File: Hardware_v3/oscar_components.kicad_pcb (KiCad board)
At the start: 4 copper layers, 71 x 100 mm, 65 parts, among them J1 SWD_Header, J10 USB_C_Receptacle, J11 MIDI_OUT, J2 ChannelA_In, J3 ChannelB_In, J4 ChannelC_In, J5 ChA_Buff_Out, J6 ChB_Buff_Out, J7 ChC_Buff_Out, J8 MIDI_IN, J9 Eurorack_10_pin_power, SW1 Left_Encoder, SW2 Right_Encoder, SW3 Reset_Button, SW4 Menu_Button, U1 STM32F446RETx, U2 ILI9341_SPI_Daughterboard, U3 MCP6004, U4 TL074, U5 LT1117-3.3, U6 6N137, Y1 8MHz

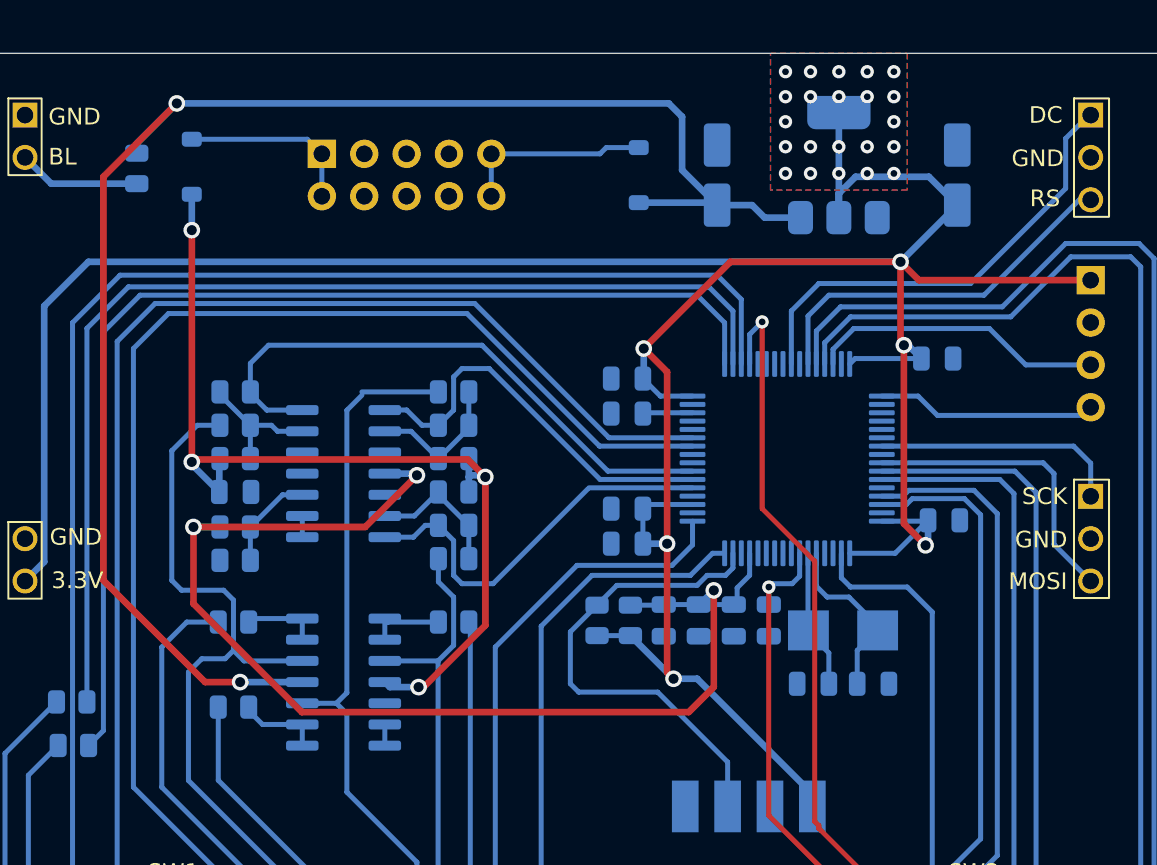
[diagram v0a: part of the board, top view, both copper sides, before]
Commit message: Folder reorganisation
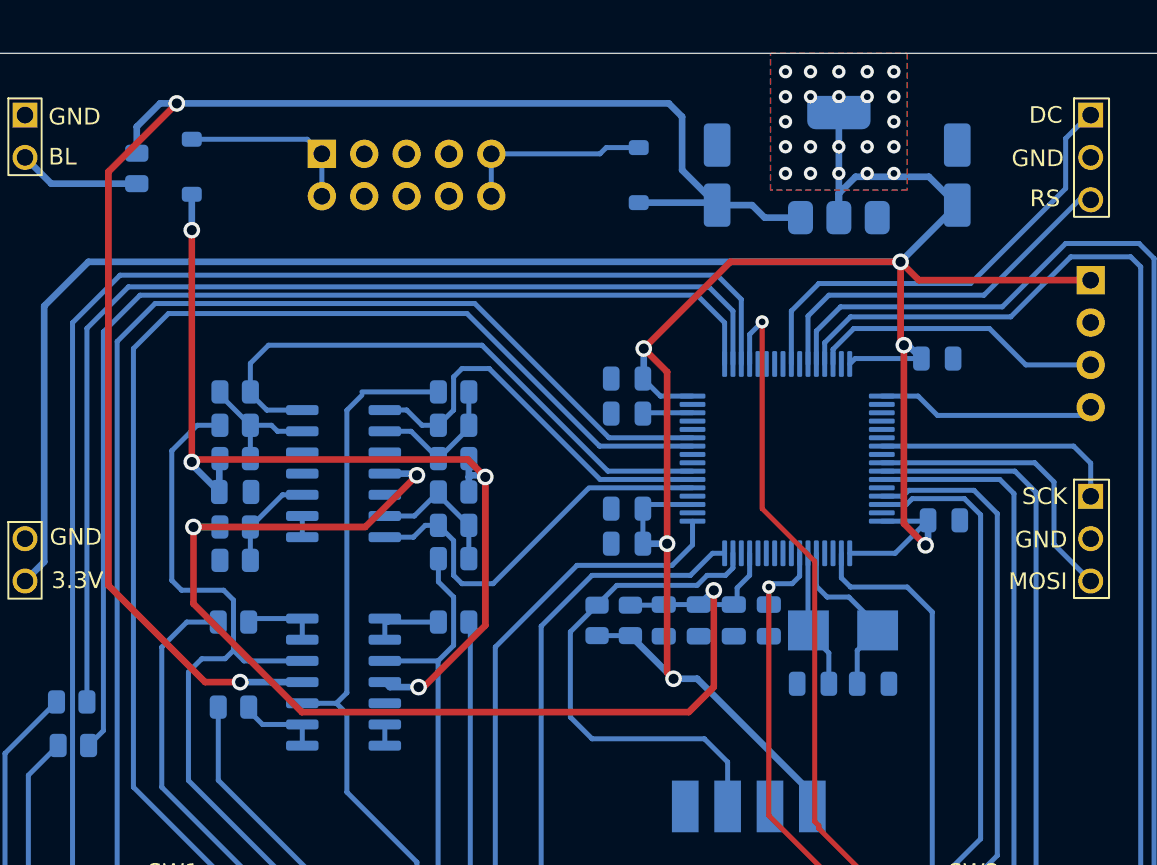
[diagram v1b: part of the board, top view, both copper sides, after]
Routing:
- net /MIDI_RX: track 29.4 -> 30.5 mm
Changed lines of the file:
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@@
 	)
 	(segment
-		(start 113.1 87.7)
-		(end 107 81.6)
+		(start 107.3 81.9)
+		(end 107.3 57.1)
 		(width 0.4)
 		(layer "F.Cu")
@@
 	)
 	(segment
-		(start 107 81.6)
-		(end 107 57.4)
+		(start 113.1 87.7)
+		(end 107.3 81.9)
 		(width 0.4)
 		(layer "F.Cu")
@@
 	)
 	(segment
-		(start 107 57.4)
+		(start 107.3 57.1)
 		(end 111.4 53)
 		(width 0.4)
@@
 	)
 	(segment
-		(start 109 55.4)
-		(end 111.4 53)
-		(width 0.4)
-		(layer "B.Cu")
-		(net 7)
-	)
-	(segment
 		(start 143.8 59.1)
 		(end 145.9 59.1)
@@
 	)
 	(segment
+		(start 109 54.4)
+		(end 110.4 53)
+		(width 0.4)
+		(layer "B.Cu")
+		(net 7)
+	)
+	(segment
 		(start 111.4 53)
 		(end 140.9 53)
@@
 	)
 	(segment
+		(start 110.4 53)
+		(end 111.4 53)
+		(width 0.4)
+		(layer "B.Cu")
+		(net 7)
+	)
+	(segment
 		(start 109 55.9875)
-		(end 109 55.4)
+		(end 109 54.4)
 		(width 0.4)
 		(layer "B.Cu")
@@
 	)
 	(segment
-		(start 143.2 81.3)
-		(end 144.30312 81.3)
+		(start 136.3 91.1)
+		(end 135 89.8)
 		(width 0.3)
 		(layer "B.Cu")
@@
 	)
 	(segment
-		(start 142.6 81.9)
-		(end 143.2 81.3)
+		(start 143.2 81.3)
+		(end 144.30312 81.3)
 		(width 0.3)
 		(layer "B.Cu")
@@
 	)
 	(segment
-		(start 140.235 88.3)
-		(end 135.5 88.3)
+		(start 142.6 81.9)
+		(end 143.2 81.3)
 		(width 0.3)
 		(layer "B.Cu")
@@
 	)
 	(segment
-		(start 144.43 95.155)
-		(end 144.43 92.495)
+		(start 144.30312 81.3)
+		(end 144.75 80.85312)
 		(width 0.3)
 		(layer "B.Cu")
@@
 	)
 	(segment
-		(start 144.30312 81.3)
-		(end 144.75 80.85312)
+		(start 135 89.8)
+		(end 135 84.6875)
 		(width 0.3)
 		(layer "B.Cu")
@@
 	)
 	(segment
-		(start 135 87.8)
-		(end 135 84.6875)
+		(start 144.43 92.495)
+		(end 143.035 91.1)
 		(width 0.3)
 		(layer "B.Cu")
@@
 	)
 	(segment
-		(start 144.43 92.495)
-		(end 140.235 88.3)
+		(start 136.6 83.0875)
+		(end 137.7875 81.9)
 		(width 0.3)
 		(layer "B.Cu")
@@
 	)
 	(segment
-		(start 135.5 88.3)
-		(end 135 87.8)
+		(start 135 84.6875)
+		(end 136.6 83.0875)
 		(width 0.3)
 		(layer "B.Cu")
@@
 	)
 	(segment
-		(start 136.6 83.0875)
-		(end 137.7875 81.9)
+		(start 143.035 91.1)
+		(end 136.3 91.1)
 		(width 0.3)
 		(layer "B.Cu")
@@
 	)
 	(segment
-		(start 135 84.6875)
-		(end 136.6 83.0875)
+		(start 144.75 80.85312)
+		(end 144.75 79.975)
 		(width 0.3)
 		(layer "B.Cu")
@@
 	)
 	(segment
-		(start 144.75 80.85312)
-		(end 144.75 79.975)
+		(start 144.43 95.155)
+		(end 144.43 92.495)
 		(width 0.3)
 		(layer "B.Cu")
@@
 	)
 	(segment
-		(start 164 79.44)
-		(end 164 75.2)
+		(start 166.2 81.64)
+		(end 164 79.44)
 		(width 0.3)
 		(layer "B.Cu")
@@
 	)
 	(segment
-		(start 163.35 74.55)
-		(end 153.675 74.55)
+		(start 164 75.7)
+		(end 162.85 74.55)
 		(width 0.3)
 		(layer "B.Cu")
@@
 	)
 	(segment
-		(start 164 75.2)
-		(end 163.35 74.55)
+		(start 164 79.44)
+		(end 164 75.7)
 		(width 0.3)
 		(layer "B.Cu")
@@
 	)
 	(segment
-		(start 166.2 81.64)
-		(end 164 79.44)
+		(start 162.85 74.55)
+		(end 153.675 74.55)
 		(width 0.3)
 		(layer "B.Cu")

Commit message: PCB Layout
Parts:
- added TP1: TestPoint, Custom_Footprints:1.3mm_Test_Point, F.Cu at (105.9, 60.4)
- added TP2: TestPoint, Custom_Footprints:1.3mm_Test_Point, F.Cu at (110.1, 60.4)
- added TP3: TestPoint, Custom_Footprints:1.3mm_Test_Point, F.Cu at (162.3, 140.0)
- added TP4: TestPoint, Custom_Footprints:1.3mm_Test_Point, F.Cu at (105.9, 51.9)
- added TP5: TestPoint, Custom_Footprints:1.3mm_Test_Point, F.Cu at (102.0, 60.4)
- J10: renamed from J11; value MIDI_OUT -> MIDI_THROUGH
- moved C15 3.50 mm to (115.0, 79.8)
- moved R10 3.50 mm to (128.1, 75.8)
- moved R11 3.50 mm to (115.0, 81.9)
- moved R12 3.50 mm to (115.0, 83.9)
- moved R13 3.50 mm to (128.1, 87.6)
- moved R14 3.50 mm to (114.9, 87.6)
- moved R15 3.50 mm to (114.9, 92.7)
- moved R2 3.50 mm to (128.1, 79.8)
- moved R3 3.50 mm to (128.1, 83.8)
- moved R4 3.50 mm to (115.0, 77.8)
- moved R5 3.50 mm to (115.0, 75.8)
- moved R6 3.50 mm to (128.1, 77.8)
- moved R7 3.50 mm to (128.1, 73.8)
- moved R8 3.50 mm to (128.1, 81.8)
- moved R9 3.50 mm to (115.0, 73.8)
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- renumbered C8 to C1, C6 to C10, C16 to C11, C7 to C12, C10 to C14, C11 to C15, C12 to C2, C1 to C3, C2 to C4, C3 to C5, C4 to C6, C9 to C7, C14 to C8, C5 to C9, D4 to D3, D3 to D4, J10 to J11, J9 to J2, J4 to J3, J2 to J4, J3 to J5, J7 to J6, J5 to J7, J6 to J8, J8 to J9, R13 to R1, R9 to R10, R16 to R11, R17 to R12, R10 to R13, R11 to R14, R12 to R15, R14 to R16, R15 to R17, R1 to R2, R2 to R3, R3 to R4, R4 to R5, R5 to R6, R6 to R7, R7 to R8, R8 to R9, SW3 to SW1, SW4 to SW2, SW1 to SW3, SW2 to SW4, U5 to U1, U1 to U3, U3 to U5
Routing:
- net +3.3V: track 202.1 -> 212.3 mm
- net -12V: track 58.4 -> 65.1 mm
- net +12V: track 96.1 -> 101.2 mm
- net /CHC_In: track 65.7 -> 61.6 mm
- net /CHB_Out: track 64.1 -> 60.0 mm
- net /CHA_In: track 86.0 -> 82.1 mm
- net /CHB_In: track 72.5 -> 68.6 mm
- net /CHA_Out: track 79.2 -> 75.4 mm
- net /CHC_Out: track 72.9 -> 69.4 mm
- net /ChC_Button: track 58.8 -> 56.4 mm
- net /ChA_Button: track 107.2 -> 104.8 mm
- net /L_ENC_BTN: track 73.1 -> 70.8 mm
- net /ChB_LED: track 66.5 -> 64.6 mm
- net +3.3VA: track 74.2 -> 76.0 mm
- net /LCD_SCK: track 14.9 -> 13.1 mm
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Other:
- board text added: "-12V"
- board text added: "12V"
- board text added: "3V3"
- board text added: "GND"
- board text added: "Oscar v3 Mountjoy Modular 2025"
- board text removed: "Oscar v3 Mountjoy Modular"

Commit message: Started working on panel
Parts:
- added J12: Debug, Connector_PinHeader_2.54mm:PinHeader_1x03_P2.54mm_Vertical, B.Cu at (166.0, 92.8)
- SW1: footprint Button_Switch_THT:SW_PUSH_6mm -> Custom_Footprints:SW_PUSH_6mm_aligned
- moved TP4 17.7 mm to (102.0, 69.2)
- moved SW1 3.70 mm to (150.4, 131.2)
- moved SW3 3.20 mm to (111.2, 105.0)
- moved SW4 3.20 mm to (159.2, 105.0)
- moved BTN1 2.60 mm to (109.4, 120.0)
- moved BTN2 2.60 mm to (124.5, 120.0)
- moved BTN3 2.60 mm to (139.4, 120.0)
- moved J3 0.80 mm to (139.4, 132.0)
- moved J4 0.80 mm to (109.4, 132.0)
- moved J5 0.80 mm to (124.4, 132.0)
- moved D4 0.30 mm to (156.4, 137.9)
- moved J11 0.30 mm to (150.5, 144.1)
- moved U2 0.20 mm to (102.1, 53.7)
- moved R19 0.10 mm to (105.1, 91.5)
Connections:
- U3 pad 51: unconnected-(U3-PC10-Pad51) -> /DEBUG1
- U3 pad 52: unconnected-(U3-PC11-Pad52) -> /DEBUG2
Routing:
- net /DEBUG1: track 0.00 -> 34.3 mm
- net /DEBUG2: track 0.00 -> 30.0 mm
- net /ChB_Button: track 107.8 -> 100.1 mm
- net /L_ENC_DN: track 85.0 -> 77.4 mm
- net Net-(BTN2-A): track 48.2 -> 53.9 mm
- net /L_ENC_UP: track 92.9 -> 88.9 mm
- net /L_ENC_BTN: track 70.8 -> 67.3 mm
- net /R_ENC_BTN: track 23.9 -> 20.7 mm
- net /R_ENC_UP: track 50.5 -> 47.3 mm
- net /R_ENC_DN: track 58.1 -> 55.1 mm
- net /ChA_Button: track 104.8 -> 102.0 mm
- net Net-(BTN3-A): track 7.11 -> 4.51 mm
- net +3.3V: track 212.3 -> 214.6 mm
- net /CHA_Out: track 75.4 -> 77.5 mm
- net /ChC_Button: track 56.4 -> 54.5 mm
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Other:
- board text added: "Debug"
- board text added: "PC10"
- board text added: "PC11"

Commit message: Control Layout change
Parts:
- SW2: footprint Button_Switch_THT:SW_PUSH_6mm -> Custom_Footprints:Low-Profile_Push_Button
- moved J9 54.2 mm to (107.6, 132.0)
- moved J10 54.2 mm to (107.6, 145.2)
- moved TP3 21.4 mm to (162.3, 118.6)
- moved J11 13.6 mm to (164.1, 144.1)
- moved SW1 13.6 mm to (164.0, 131.2)
- moved BTN1 12.6 mm to (122.0, 120.0)
- moved BTN2 12.6 mm to (137.1, 120.0)
- moved BTN3 12.6 mm to (152.0, 120.0)
- moved J3 12.6 mm to (152.0, 132.0), turned to 90 degrees
- moved J4 12.6 mm to (122.0, 132.0), turned to 90 degrees
- moved J5 12.6 mm to (137.0, 132.0), turned to 90 degrees
- moved J6 12.6 mm to (152.0, 145.2), turned to 90 degrees
- moved J7 12.6 mm to (122.0, 145.2), turned to 90 degrees
- moved J8 12.6 mm to (137.0, 145.2), turned to 90 degrees
- moved D4 7.83 mm to (164.2, 137.2), turned to 90 degrees
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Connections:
- SW2 pad 1: /MENU -> GND
- SW2 pad 2: GND -> /MENU
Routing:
- net /MIDI_DATA: track 55.7 -> 83.8 mm, vias 0 -> 1
- net GND: track 0.00 -> 25.5 mm, vias 6 -> 20
- net /ChC_Button: track 54.5 -> 77.7 mm
- net /MIDI_VREF: track 43.0 -> 65.3 mm, vias 0 -> 1
- net +3.3V: track 214.6 -> 235.1 mm
- net /ChC_LED: track 75.2 -> 61.4 mm
- net Net-(BTN1-A): track 44.6 -> 54.5 mm
- net /MENU: track 39.7 -> 31.0 mm
- net /ChB_Button: track 100.1 -> 108.5 mm, vias 0 -> 1
- net Net-(BTN3-A): track 4.51 -> 12.1 mm
- net /USB_DP: track 134.7 -> 128.7 mm
- net /CHC_In: track 62.3 -> 68.0 mm
- net /CHC_Out: track 69.4 -> 74.0 mm
- net /CHA_Out: track 77.5 -> 81.8 mm
- net /ChA_Button: track 102.0 -> 106.3 mm
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
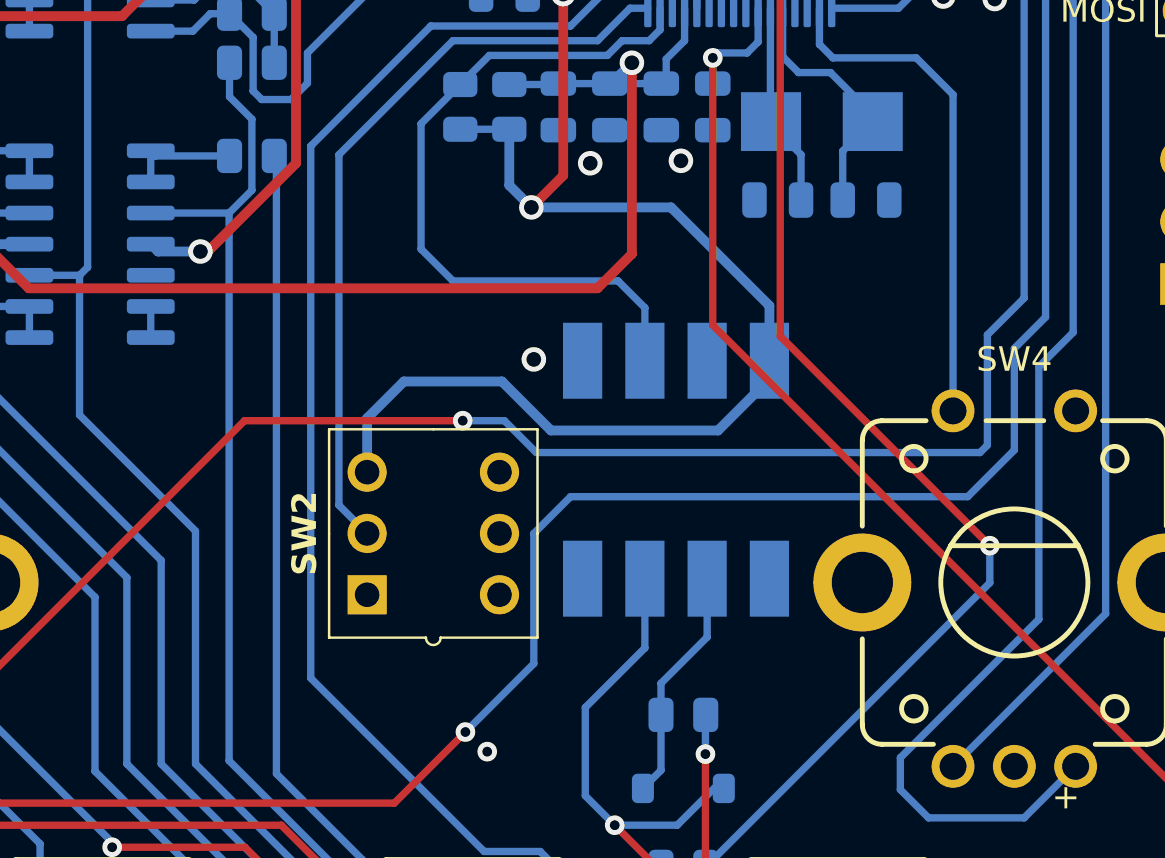
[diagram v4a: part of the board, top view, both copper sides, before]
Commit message: Started adding JLC part numbers; changed optocoupler to H11L1
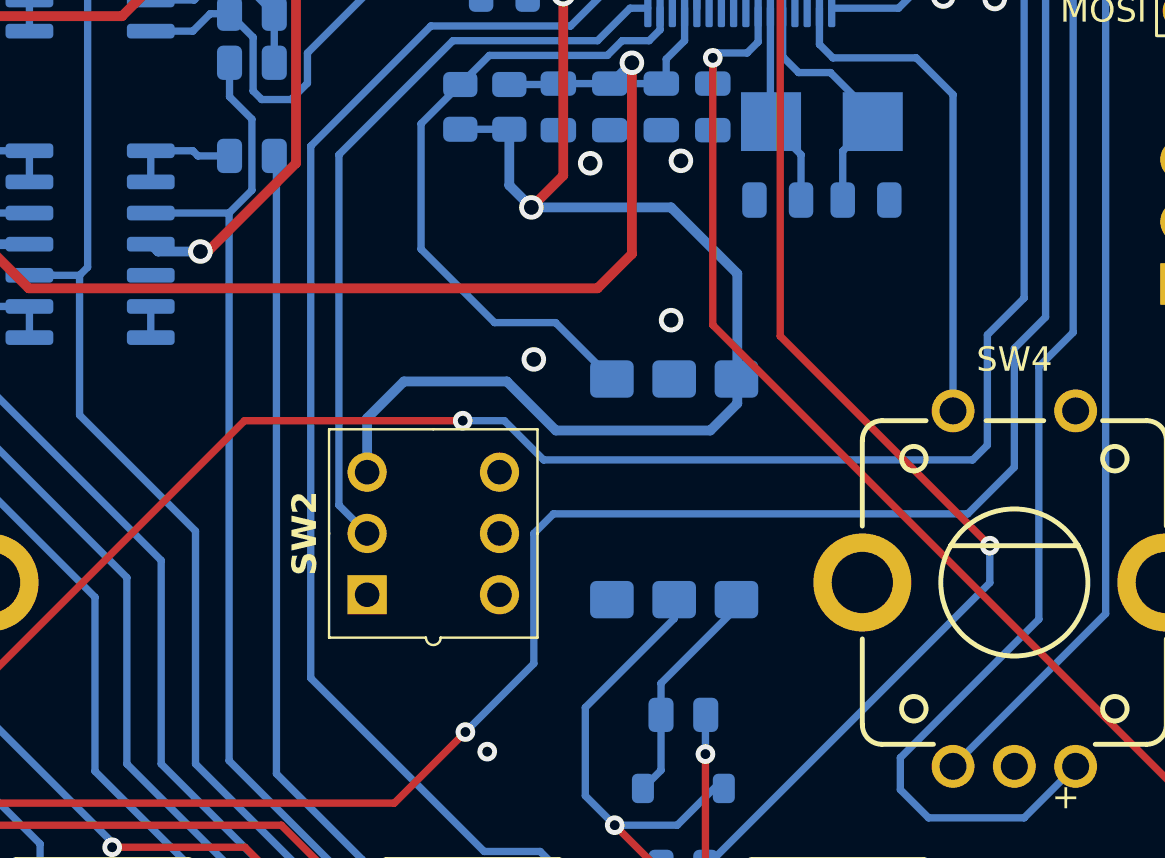
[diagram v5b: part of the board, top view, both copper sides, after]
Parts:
- C8: value 10uF -> 22uF
- R17: value 10k -> 470
- U6: value 6N137 -> H11L1; footprint Package_DIP:DIP-8_W8.89mm_SMDSocket_LongPads -> Custom_Footprints:H11L1
- moved U6 5.85 mm to (147.9, 105.7)
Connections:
- U6 pad 1: unconnected-(U6-NC-Pad1) -> Net-(D3-K)
- U6 pad 2: Net-(D3-K) -> /MIDI_DATA
- U6 pad 3: /MIDI_DATA -> unconnected-(U6-Pad3)
- U6 pad 4: unconnected-(U6-NC-Pad4) -> /MIDI_RX
- U6 pad 6: /MIDI_RX -> +3.3V
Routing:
- net /MIDI_RX: track 29.6 -> 27.3 mm
- net +3.3V: track 235.1 -> 233.9 mm
- net GND: vias 20 -> 21

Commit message: More layout
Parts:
- SW2: footprint Custom_Footprints:Low-Profile_Push_Button -> Custom_Footprints:SW_PUSH_6mm_aligned
- moved R20 5.97 mm to (149.5, 112.0), turned to -90 degrees
- moved R16 2.06 mm to (147.0, 112.0), turned to -90 degrees
- moved SW2 2.00 mm to (135.5, 101.0)
- moved D3 1.98 mm to (144.3, 112.0), turned to -90 degrees
- moved SW3 1.00 mm to (111.2, 104.0)
- moved SW4 1.00 mm to (159.2, 104.0)
- turned BTN1 to 180 degrees
- turned C4 to 180 degrees
- turned C5 to 0 degrees
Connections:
- SW2 pad 1: GND -> /MENU
- SW2 pad 2: /MENU -> GND
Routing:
- net /MIDI_DATA: track 83.4 -> 123.5 mm, vias 1 -> 0
- net /MIDI_VREF: track 65.3 -> 104.5 mm, vias 1 -> 0
- net +3.3V: track 233.9 -> 212.8 mm
- net /ChC_Button: track 77.7 -> 65.2 mm
- net /ChA_Button: track 106.3 -> 112.6 mm
- net Net-(BTN1-A): track 54.5 -> 49.1 mm
- net /ChC_LED: track 61.4 -> 56.2 mm
- net /CHA_Out: track 81.8 -> 78.3 mm
- net /CHC_Out: track 74.0 -> 70.9 mm
- net /L_ENC_UP: track 89.3 -> 86.6 mm
- net /L_ENC_DN: track 78.5 -> 80.7 mm
- net /MENU: track 31.0 -> 32.4 mm
- net /R_ENC_UP: track 47.3 -> 46.3 mm
- net /R_ENC_BTN: track 20.7 -> 19.7 mm
- net /L_ENC_BTN: track 67.3 -> 66.3 mm
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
